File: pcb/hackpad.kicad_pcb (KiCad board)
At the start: 2 copper layers, 62.5 x 62.5 mm, 38 parts, among them SW1 SW_Push, SW2 SW_Push, SW3 RotaryEncoder_Switch, SW4 SW_Push, SW5 SW_Push, SW6 SW_Push, SW7 SW_Push, SW8 SW_Push, SW9 SW_Push, U1 XIAO-RP2040-DIP

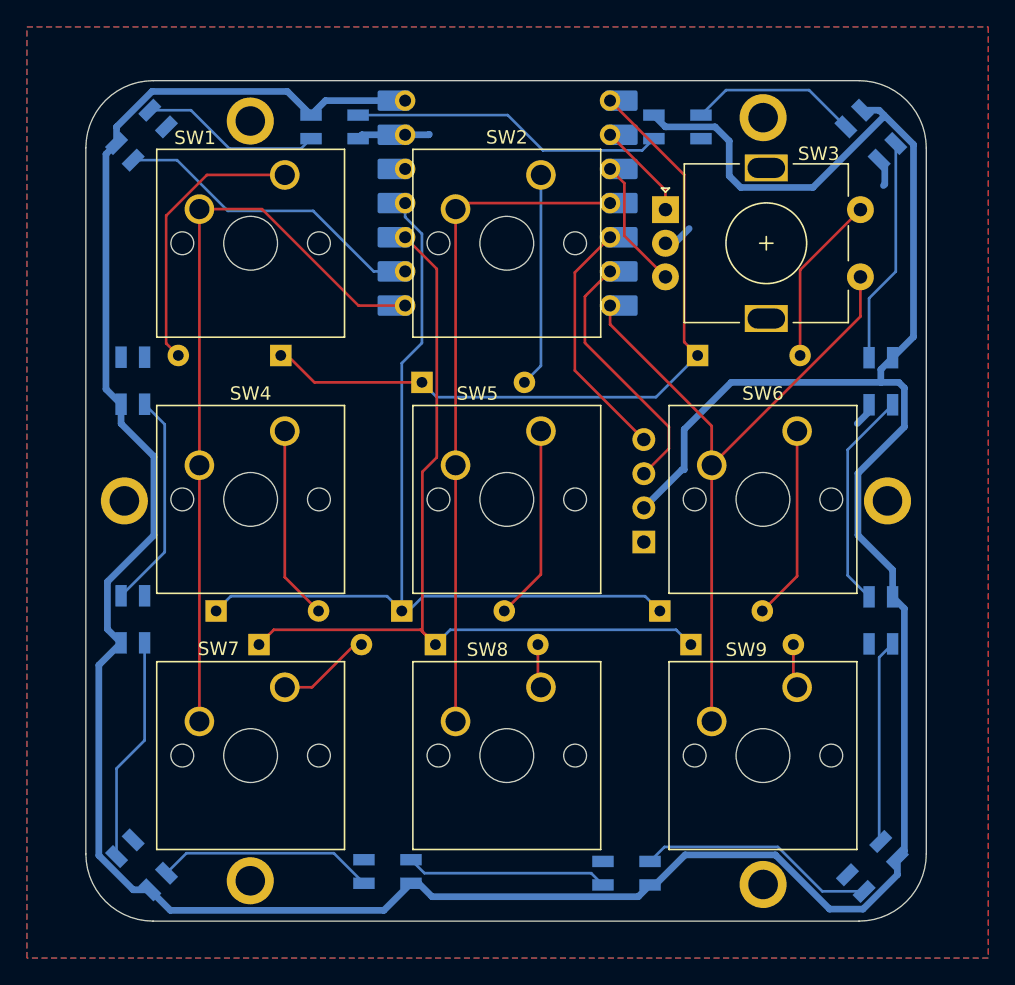
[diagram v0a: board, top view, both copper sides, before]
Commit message: Fix OLED voltage
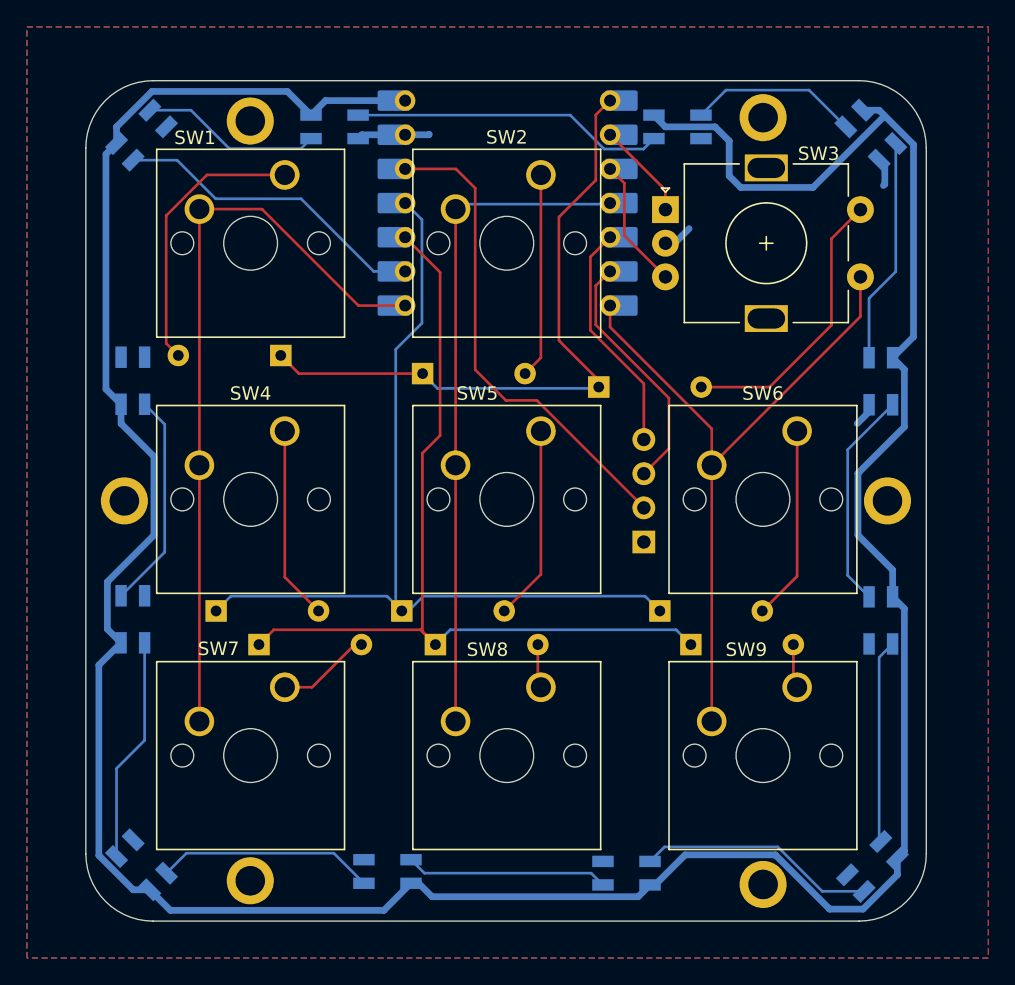
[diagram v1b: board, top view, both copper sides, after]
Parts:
- moved D3 7.72 mm to (154.2, 91.8)
- moved D2 0.65 mm to (141.1, 90.8)
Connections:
- OL1 pad 2: +5V -> +3V3
- U1 pad 12: unconnected-(U1-3V3-Pad12) -> +3V3
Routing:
- net +3V3: track 0.00 -> 36.1 mm
- net +5V: track 259.7 -> 235.0 mm
- net EN_SW1: track 12.7 -> 21.1 mm
- net ROW0: track 55.2 -> 49.3 mm
- net OL_SDA: track 18.3 -> 17.3 mm
- net Net-(D2-A): track 15.9 -> 15.3 mm
- net OL_SCL: track 19.2 -> 18.5 mm
- net COL1: track 49.8 -> 50.4 mm

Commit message: Update hackpad
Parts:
- moved D12 0.45 mm to (160.5, 72.5)
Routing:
- net Net-(D12-DOUT): track 12.7 -> 26.4 mm
- net Net-(D18-DOUT): track 16.2 -> 25.5 mm
- net Net-(D15-DOUT): track 15.2 -> 24.1 mm
- net +5V: track 235.0 -> 227.3 mm
- net Net-(D20-DOUT): track 16.2 -> 23.9 mm
- net Net-(D10-DOUT): track 13.5 -> 21.1 mm
- net Net-(D14-DOUT): track 16.3 -> 23.9 mm
- net Net-(D16-DOUT): track 17.7 -> 25.3 mm
- net Net-(D13-DOUT): track 16.8 -> 24.2 mm
- net Net-(D17-DOUT): track 15.1 -> 22.4 mm
- net Net-(D11-DOUT): track 23.5 -> 30.6 mm
- net Net-(D19-DOUT): track 16.8 -> 23.7 mm
- net GND: track 11.5 -> 15.6 mm
- net LED: track 23.6 -> 22.2 mm
